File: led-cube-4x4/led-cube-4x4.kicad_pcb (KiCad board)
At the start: 2 copper layers, 160 x 99.7 mm, 40 parts, among them J1 USB, P0 CONN_1, P1 CONN_1, P10 CONN_1, P11 CONN_1, P12 CONN_1, P13 CONN_1, P14 CONN_1, P15 CONN_1, P16 CONN_1, P17 CONN_3X2, P18 CONN_1, P19 CONN_1, P2 CONN_1, P20 CONN_1, P21 CONN_1, P22 CONN_1, P23 CONN_1, P24 CONN_1, P25 CONN_1, P26 CONN_1, P3 CONN_1, P4 CONN_1, P5 CONN_1, P6 CONN_1, P7 CONN_1, P8 CONN_1, P9 CONN_1, Q1 MOS_P, Q2 MOS_P, Q3 MOS_P, Q4 MOS_P, SW1 SW_PUSH, U1 ATTINY841-SOIC, U2 TLC5925, U3 FT232RL

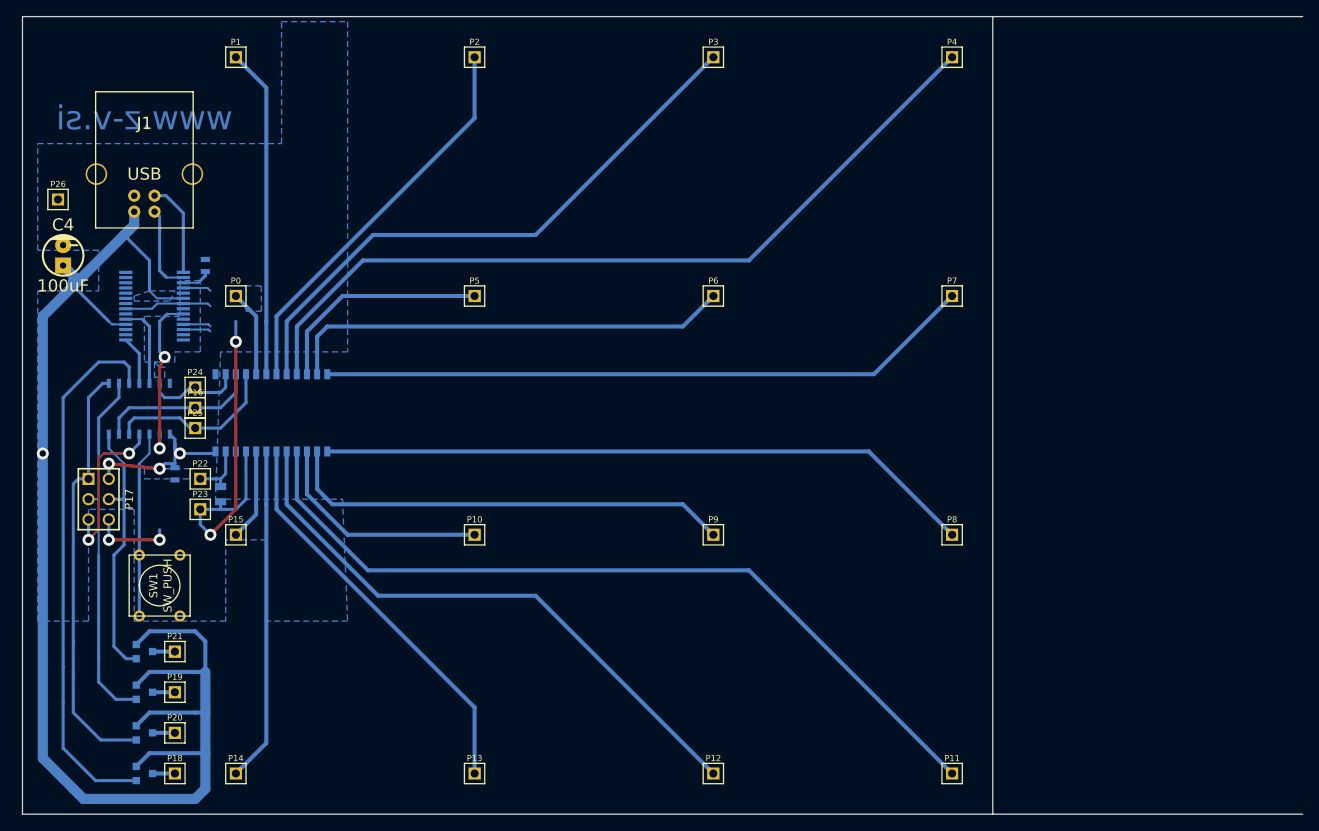
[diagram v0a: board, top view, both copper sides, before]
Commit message: Better copper coverage on pcb.
Signed-off-by: matematik7 <domen.ipavec@z-v.si>
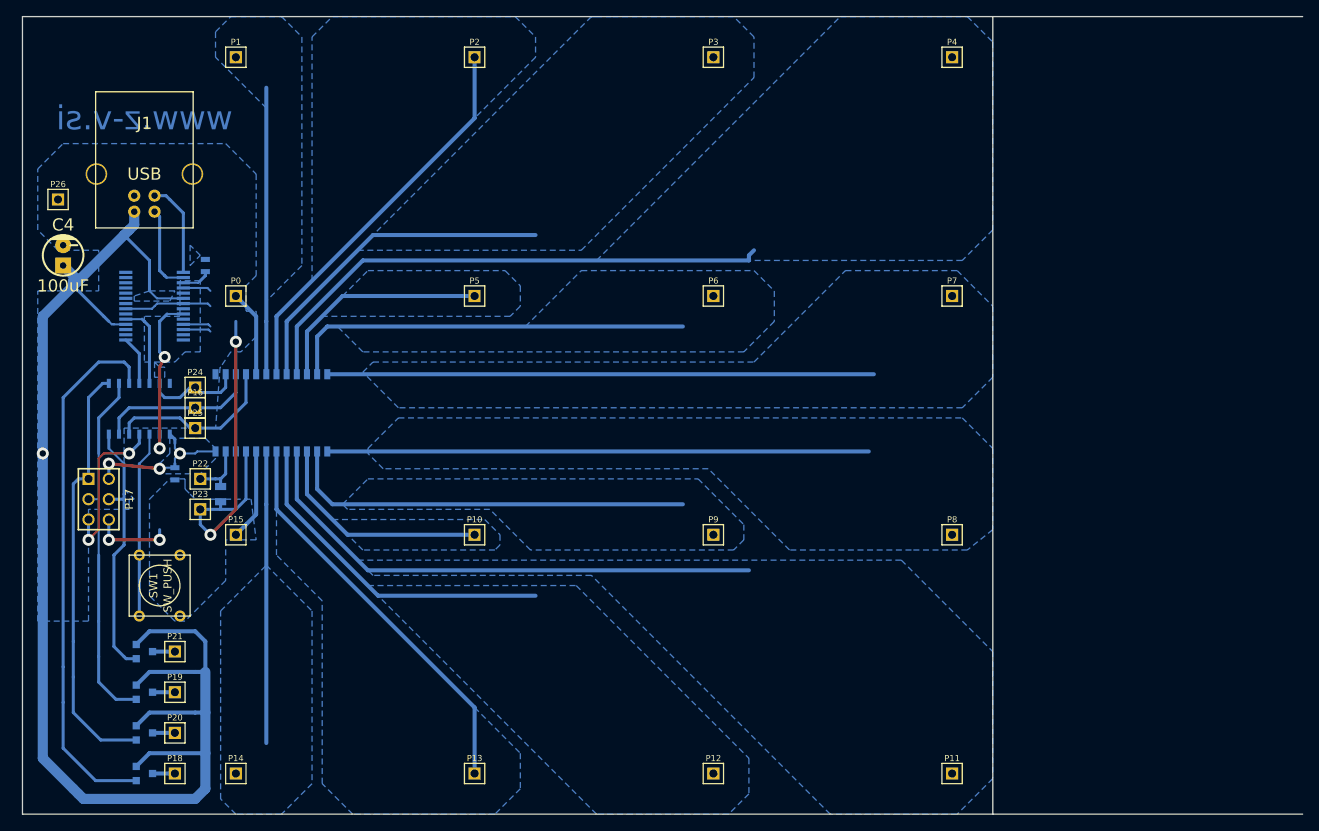
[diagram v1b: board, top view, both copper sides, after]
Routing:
- net N-0000047: track 102.1 -> 66.2 mm
- net N-0000016: track 101.8 -> 67.4 mm
- net N-0000015: track 73.6 -> 42.2 mm
- net N-0000046: track 73.9 -> 42.5 mm
- net N-0000034: track 82.4 -> 67.7 mm
- net N-0000036: track 82.2 -> 68.3 mm
- net N-0000044: track 41.8 -> 36.4 mm
- net N-0000033: track 56.6 -> 51.2 mm
- net N-0000013: track 41.2 -> 35.8 mm
- net N-0000037: track 56.3 -> 50.9 mm
- net +5V: track 199.9 -> 199.2 mm
- added copper zone on B.Cu, net +5V
- added copper zone on B.Cu, net N-0000013
- added copper zone on B.Cu, net N-0000014
- added copper zone on B.Cu, net N-0000015
- added copper zone on B.Cu, net N-0000016
- added copper zone on B.Cu, net N-0000028
- added copper zone on B.Cu, net N-0000033
- added copper zone on B.Cu, net N-0000034
- added copper zone on B.Cu, net N-0000036
- added copper zone on B.Cu, net N-0000037
- added copper zone on B.Cu, net N-0000039
- added copper zone on B.Cu, net N-0000044
- added copper zone on B.Cu, net N-0000045
- added copper zone on B.Cu, net N-0000046
- added copper zone on B.Cu, net N-0000047
